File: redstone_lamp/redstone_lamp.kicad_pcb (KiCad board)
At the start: 2 copper layers, 40 x 40 mm, 76 parts, among them J1 1x4_Pogo, J2 1x4_Pogo, J3 1x4_Pogo, J4 1x4_Pogo, J5 1x4_Pogo, J6 1x4_Pogo, J7 1x4_Pogo, J8 1x4_Pogo, J9 2.54mm_ProgrammingPin, Q1 BC108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

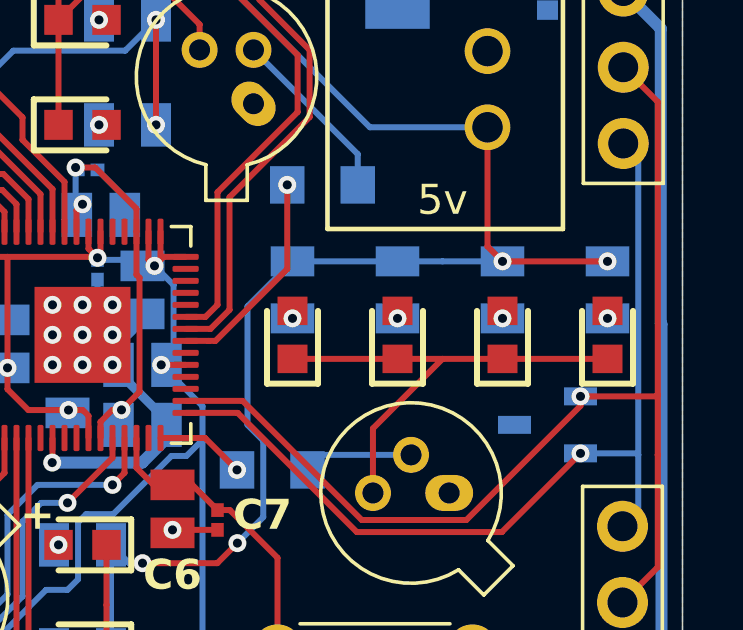
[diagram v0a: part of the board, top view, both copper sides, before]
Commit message: remove all unecessary components in schematic
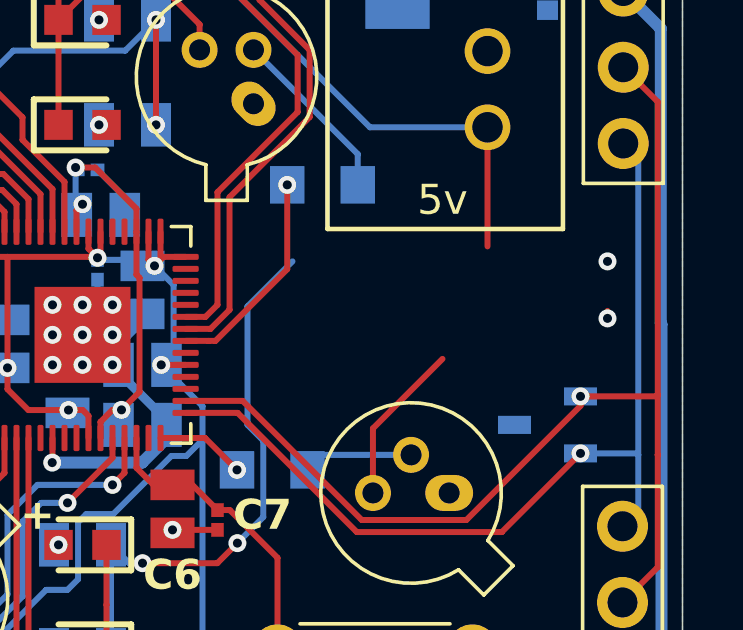
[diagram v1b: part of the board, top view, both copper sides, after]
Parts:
- removed the 200 at (149.0, 53.5)
- removed D5, D6, D7, D8: LED, SamacSys_Parts:LEDC1608X115N
- removed R5, R7, R8: 200, SamacSys_Parts:CRCW1210200RJNEAIF
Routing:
- net /5V_LOCAL: track 103.9 -> 92.7 mm, vias 9 -> 8
- net Net-(D5-K): track 15.9 -> 5.43 mm
- net Net-(D8-A): track 0.25 -> 0.00 mm, vias 1 -> 0
- net Net-(D7-A): track 0.25 -> 0.00 mm, vias 1 -> 0
- net Net-(D6-A): track 0.25 -> 0.00 mm, vias 1 -> 0

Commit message: finalize redstone lamp design
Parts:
- removed the 1k at (128.3, 58.5)
- removed the 1k at (143.0, 50.0)
- removed the 1k at (141.3, 59.5)
- removed the 1k at (131.5, 61.7)
- removed the 200 at (124.5, 56.5)
- removed the 200 at (135.0, 65.5)
- removed D10, D11, D12, D13, D14, D15, D16, D9: LED, SamacSys_Parts:LEDC1608X115N
- removed Q2, Q3, Q4: BC108, Package_TO_SOT_THT:TO-18-3
- removed R10, R12, R13, R14, R16, R9: 200, SamacSys_Parts:CRCW1210200RJNEAIF
- added 1k: 1k, SamacSys_Parts:ERJ-UP6D1001V, B.Cu at (140.5, 58.2)
- D18, D20: moved to F.Cu
- moved R3 23.2 mm to (133.4, 67.5), turned to 0 degrees
- moved D3 23.0 mm to (135.0, 67.5), turned to 180 degrees
- moved D2 18.8 mm to (147.5, 55.0), turned to 90 degrees
- moved R2 16.7 mm to (147.5, 53.5), turned to -90 degrees
- moved R4 16.4 mm to (122.5, 56.5), turned to 90 degrees
- moved D4 14.3 mm to (122.5, 55.0), turned to -90 degrees
- moved Q1 7.81 mm to (142.0, 55.0), turned to 0 degrees
- moved 200 5.00 mm to (136.5, 42.5)
- moved D1 5.00 mm to (135.0, 42.5)
- moved D20 1.50 mm to (133.0, 70.5), turned to 90 degrees
- moved D18 0.50 mm to (150.5, 57.5)
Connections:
- U1 pad 14: Net-(U1-GPIO11) -> unconnected-(U1-GPIO11-Pad14)
- U1 pad 15: Net-(U1-GPIO12) -> unconnected-(U1-GPIO12-Pad15)
- U1 pad 28: Net-(U1-GPIO17) -> unconnected-(U1-GPIO17-Pad28)
- U1 pad 29: /E_RX -> /E_TX
- U1 pad 30: /E_TX -> /E_RX
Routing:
- net Net-(D1-K): track 16.8 -> 59.7 mm, vias 0 -> 5
- net Net-(D10-K): track 17.8 -> 0.00 mm
- net Net-(D13-K): track 16.7 -> 0.00 mm
- net /5V_LOCAL: track 92.7 -> 83.8 mm, vias 8 -> 10
- net Net-(D5-K): track 5.43 -> 0.00 mm
- net Net-(Q4-B): track 5.02 -> 0.00 mm
- net Net-(U1-GPIO23): track 7.19 -> 2.64 mm
- net Net-(Q2-B): track 3.66 -> 0.00 mm
- net Net-(Q3-B): track 3.65 -> 0.00 mm
- net /E_RX: track 31.0 -> 27.6 mm, vias 1 -> 0
- net Net-(U1-GPIO17): track 2.99 -> 0.00 mm, vias 1 -> 0
- net GND: track 19.3 -> 16.4 mm, vias 18 -> 20
- net Net-(U1-GPIO12): track 2.44 -> 0.00 mm, vias 1 -> 0
- net Net-(U1-GPIO11): track 2.44 -> 0.00 mm
- net /N_RX: track 34.1 -> 31.9 mm
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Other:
- board text removed: "+"

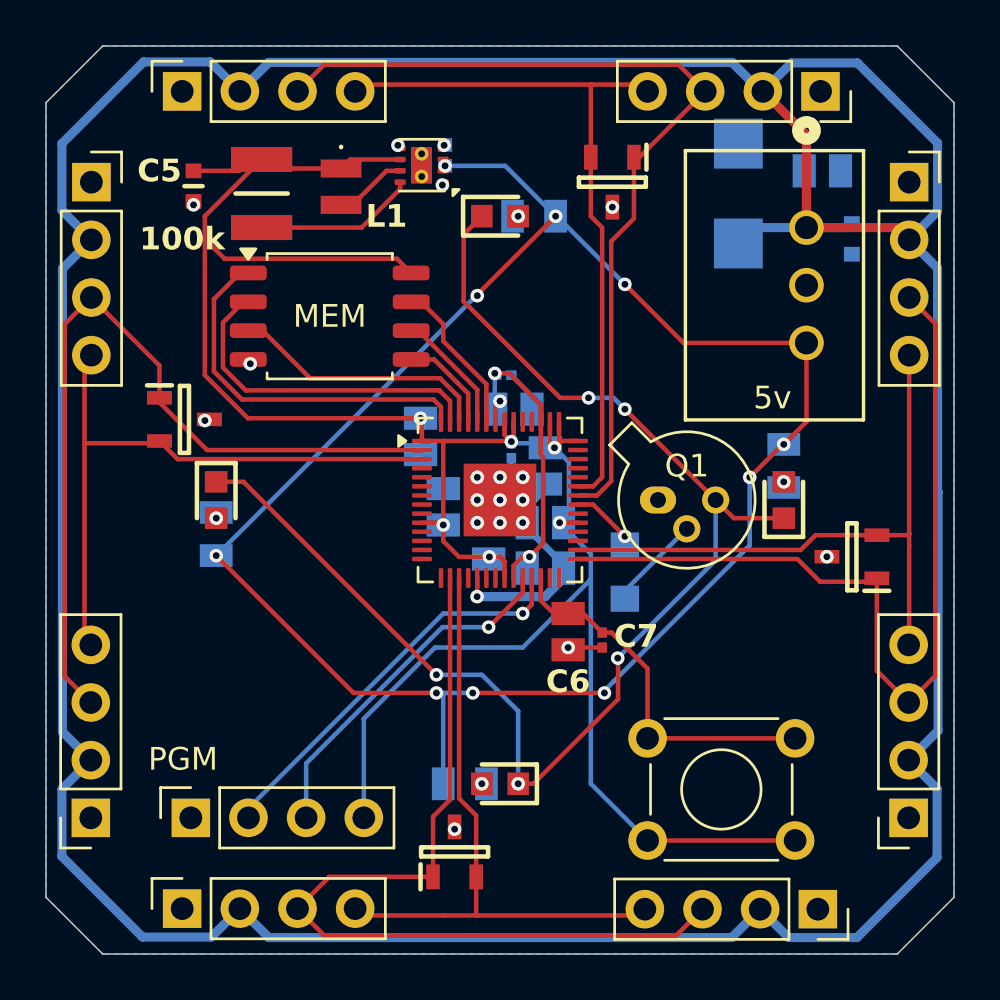
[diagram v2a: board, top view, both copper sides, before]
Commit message: switch redstone lamp transistor to mmbt3904
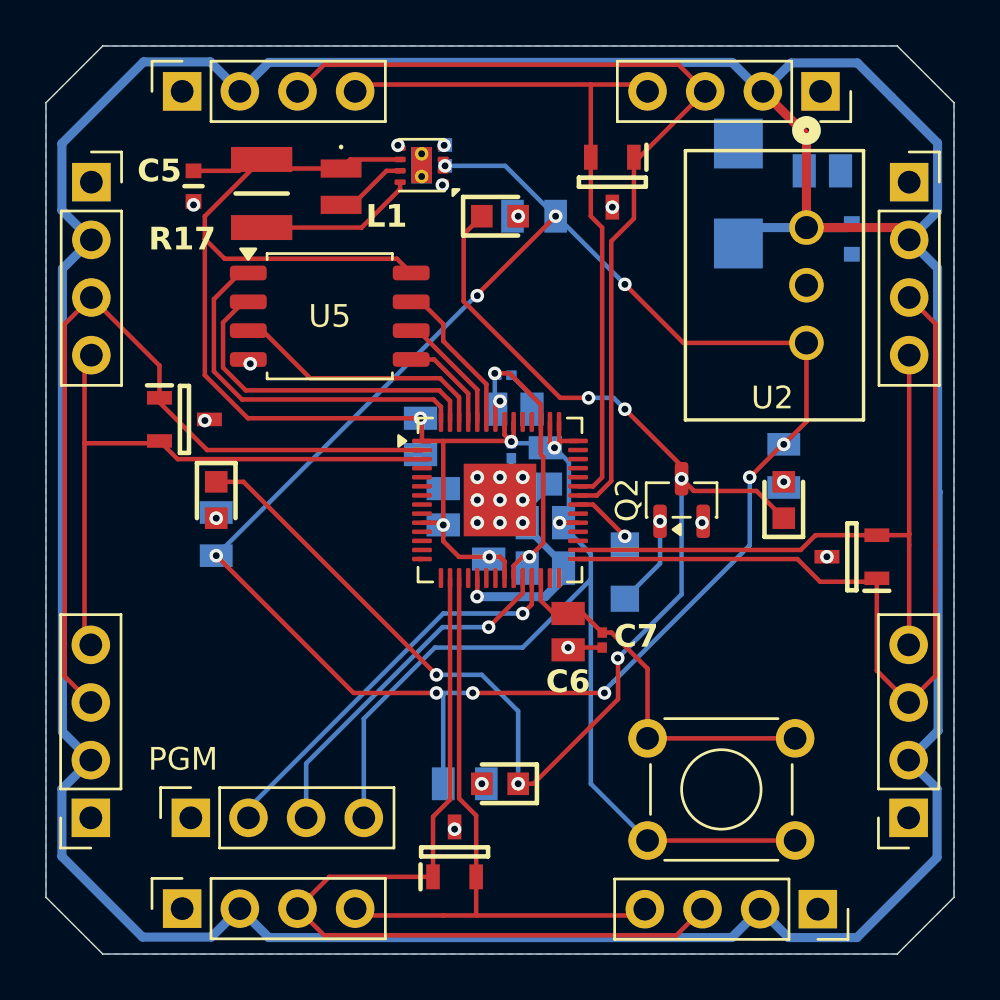
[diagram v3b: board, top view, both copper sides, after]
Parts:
- removed Q1: BC108, Package_TO_SOT_THT:TO-18-3
- added Q2: MMBT3904, Package_TO_SOT_SMD:SOT-23, F.Cu at (143.0, 55.0)
- renumbered 200 to R1, 100k to R17, 1k to R5, 5v to U2, MEM to U5
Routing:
- net Net-(D1-K): track 59.7 -> 60.4 mm, vias 5 -> 6
- net Net-(Q2-B): track 4.21 -> 4.05 mm, vias 0 -> 1
- net GND: track 16.4 -> 16.5 mm, vias 20 -> 21
